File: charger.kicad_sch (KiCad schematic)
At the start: 16 parts, among them U8 BQ24295

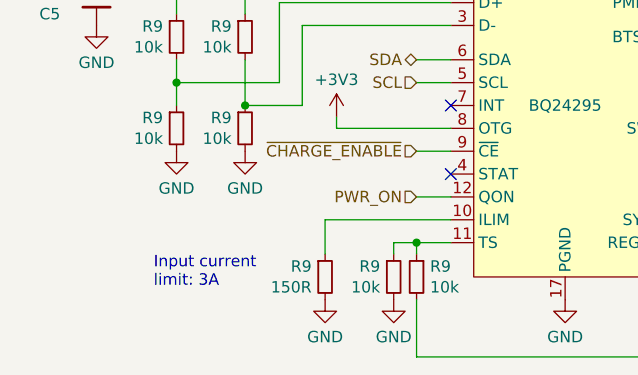
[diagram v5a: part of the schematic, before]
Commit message: DFM and 2A input current limit
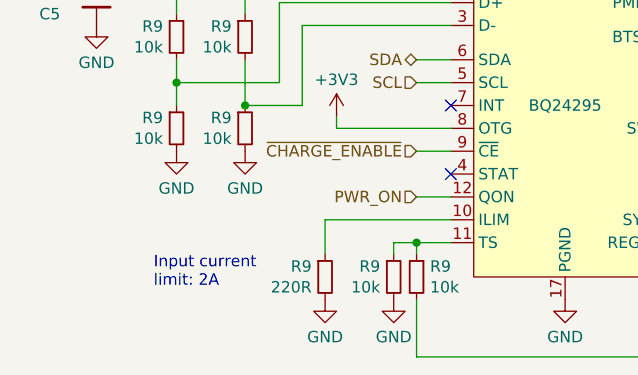
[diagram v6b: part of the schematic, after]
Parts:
- R9: value 150R -> 220R; LCSC C25082 -> C25091
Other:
- note added: "Input current limit: 2A"
- note removed: "Input current limit: 3A"
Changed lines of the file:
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@@
     (stroke (width 0) (type default))
   )
-  (text "Input current\nlimit: 3A" (at 100.33 76.2 0)
+  (text "Input current\nlimit: 2A" (at 100.33 76.2 0)
     (effects (font (size 1.27 1.27)) (justify left bottom))
   )
@@
       (effects (font (size 1.27 1.27)) (justify right))
     )
-    (property "Value" "150R" (at 117.8814 76.073 0)
+    (property "Value" "220R" (at 117.8814 76.073 0)
       (effects (font (size 1.27 1.27)) (justify right))
     )
@@
       (effects (font (size 1.27 1.27)) hide)
     )
-    (property "LCSC" "C25082" (at 119.38 74.93 0)
-      (effects (font (size 1.27 1.27)) hide)
-    )
+    (property "LCSC" "C25091" (at 119.38 74.93 0)
+      (effects (font (size 1.27 1.27)) hide)
+    )
